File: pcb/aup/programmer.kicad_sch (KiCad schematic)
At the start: 6 parts, among them U11 FT2232HQ, U12 93LC56BT-I/OT, U13 MX25L3233FM2, Y1 12MHz/20pf

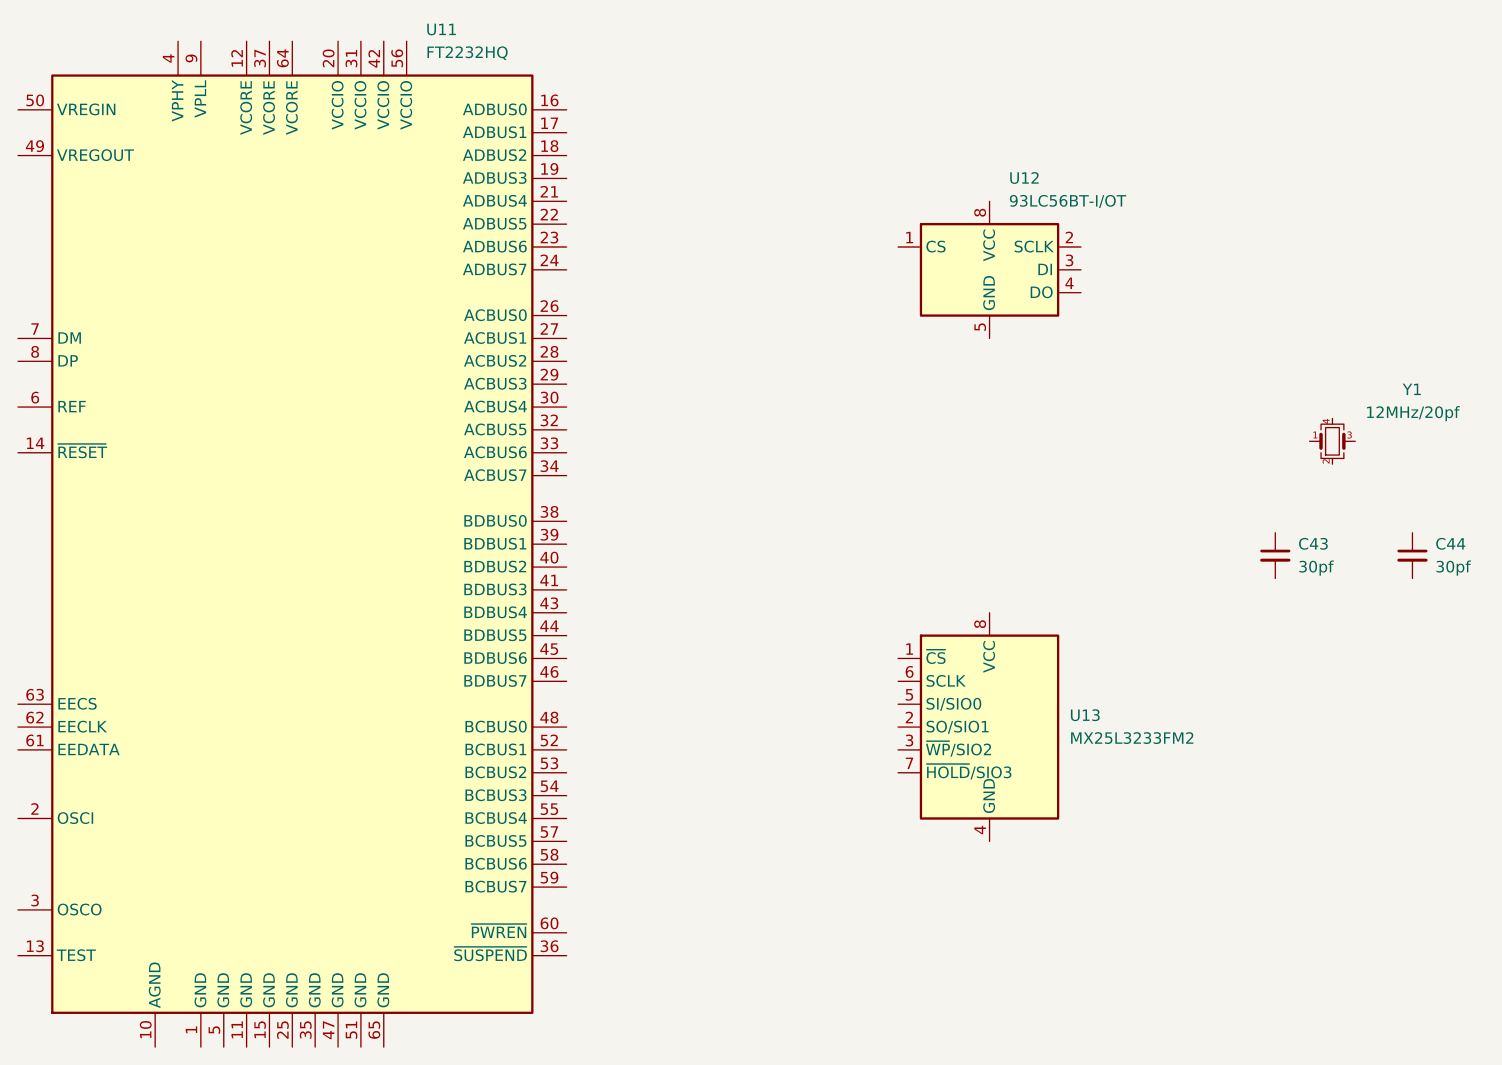
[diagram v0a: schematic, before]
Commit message: Fix L1 footprint and add reg and ftdi models
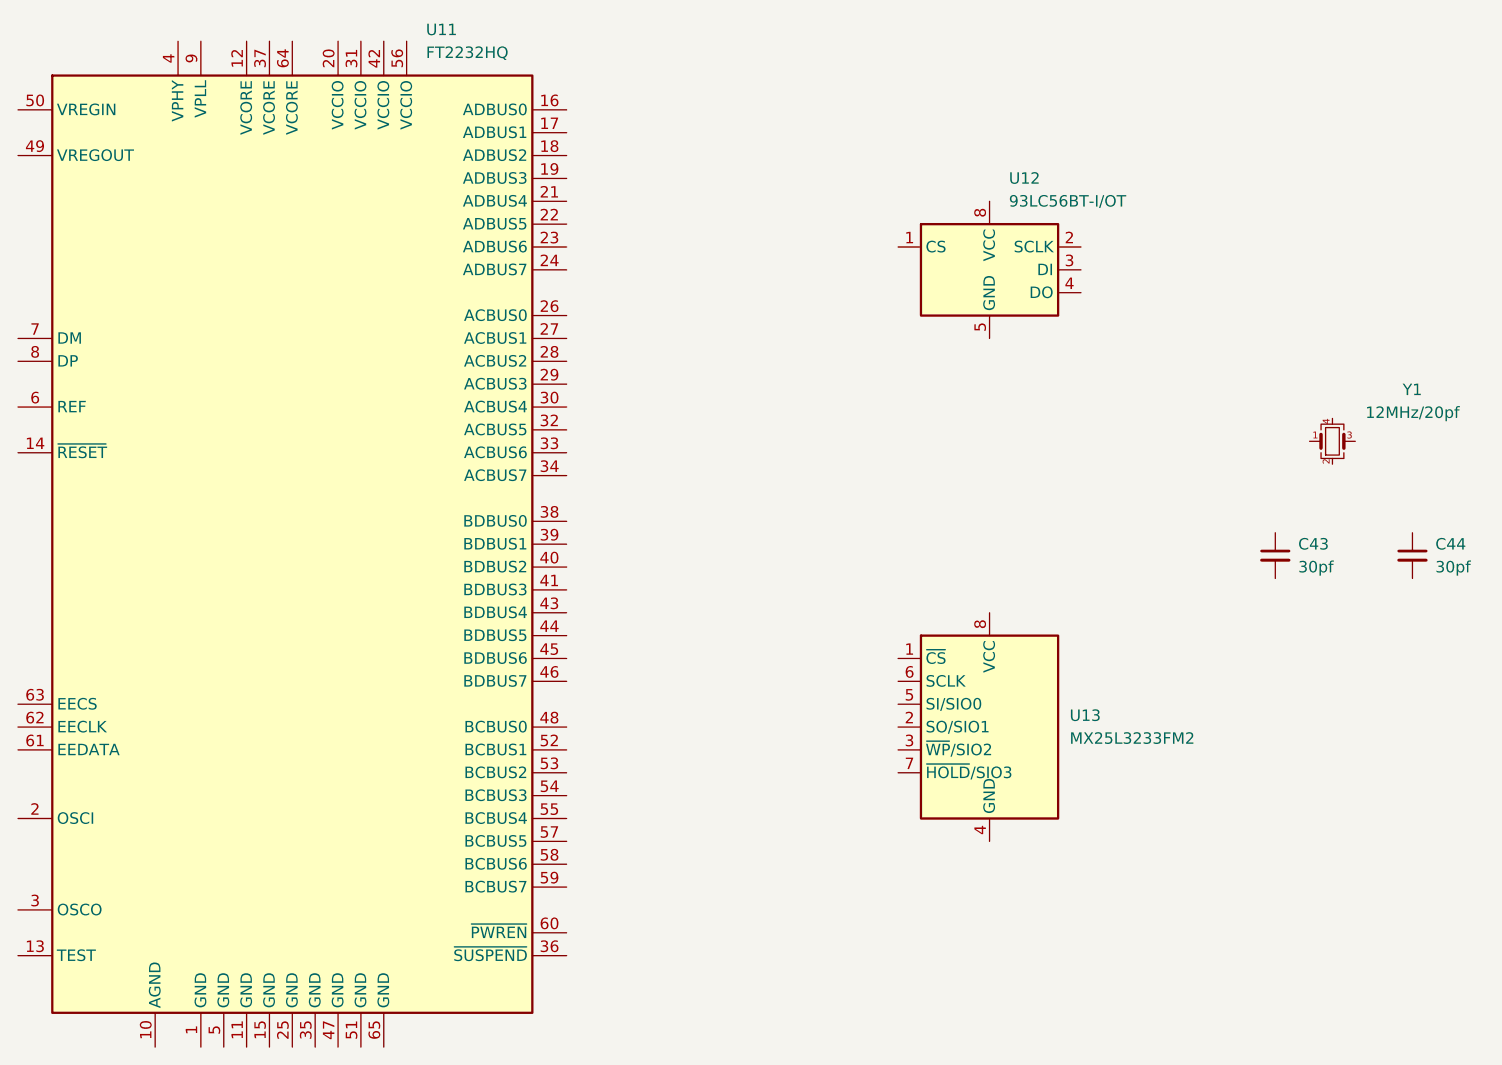
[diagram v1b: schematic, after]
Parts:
- U11: footprint Package_DFN_QFN:QFN-64-1EP_9x9mm_P0.5mm_EP4.35x4.35mm -> !Misc:FT2232HQ; Digi-Key Part Number (none) -> 768-1025-1-ND; LCSC Part # (none) -> C193662
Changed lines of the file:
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@@
 			)
 		)
-		(property "Footprint" "Package_DFN_QFN:QFN-64-1EP_9x9mm_P0.5mm_EP4.35x4.35mm"
+		(property "Footprint" "!Misc:FT2232HQ"
 			(at 77.47 87.63 0)
 			(effects
@@
 			(at 77.47 87.63 0)
 			(effects
+				(font
+					(size 1.27 1.27)
+				)
+				(hide yes)
+			)
+		)
+		(property "LCSC Part #" "C193662 "
+			(at 77.47 87.63 0)
+			(effects
+				(font
+					(size 1.27 1.27)
+				)
+				(hide yes)
+			)
+		)
+		(property "Digi-Key Part Number" "768-1025-1-ND"
+			(at 77.47 87.63 0)
+			(effects

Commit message: Start working out GTP diff pair routing
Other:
- note added: "this doesn't match footprint"
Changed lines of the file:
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@@
 	(generator_version "9.0")
 	(paper "A4")
+	(text "this doesn't match footprint\n"
+		(exclude_from_sim no)
+		(at 180.848 56.896 0)
+		(effects
+			(font
+				(size 1.27 1.27)
+			)
+		)
+	)
 	(symbol
 		(lib_id "!Misc:93LC56BT-I/OT")
